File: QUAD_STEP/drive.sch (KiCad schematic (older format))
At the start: 17 parts, among them U3 TMC5160-TA

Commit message: beginning layout
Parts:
- C17: footprint (none) -> Capacitor_SMD:C_0603_1608Metric_Pad1.05x0.95mm_HandSolder
- C18: footprint (none) -> Capacitor_SMD:C_0603_1608Metric_Pad1.05x0.95mm_HandSolder; ALTERNATE (none) -> EMK107BJ225KA-T,587-1430-1-ND; DPN (none) -> 1276-1040-1-ND
- C20: footprint (none) -> CUSTOM:CAPAE1350X1400N_EEVFK1J151Q
- R86, R87, R88, R89, R90: footprint (none) -> Resistor_SMD:R_0603_1608Metric_Pad1.05x0.95mm_HandSolder
- U3: footprint eTQFP48_9x9 -> CUSTOM:TMC5160-TA; DPN (none) -> 1460-1249-ND; MPN (none) -> TMC5160-TA
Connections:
- net GND: now also C18.1; no longer C18.2
- net at U3.3 (12VOUT): now also C18.2; no longer C18.1

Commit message: complebegan adding 3D files
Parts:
- C16, C19: footprint Capacitor_SMD:C_0603_1608Metric -> Capacitor_SMD:C_0603_1608Metric_Pad1.05x0.95mm_HandSolder
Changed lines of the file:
@@
 AR Path="/5E50B0AB/5E4B8E3D" Ref="U5"  Part="1"
 AR Path="/5E50B60F/5E4B8E3D" Ref="U6"  Part="1"
-F 0 "U6" H 5400 1737 60  0000 C CNN
+F 0 "U3" H 5400 1737 60  0000 C CNN
 F 1 "TMC5160-TA" H 5400 1631 60  0000 C CNN
 F 2 "CUSTOM:TMC5160-TA" H 5400 1590 60  0001 C CNN
@@
 AR Path="/5E50B0AB/5E4B8E77" Ref="C60"  Part="1"
 AR Path="/5E50B60F/5E4B8E77" Ref="C77"  Part="1"
-F 0 "C77" H 7015 2296 50  0000 L CNN
+F 0 "C26" H 7015 2296 50  0000 L CNN
 F 1 "22n" H 7015 2205 50  0000 L CNN
 F 2 "Capacitor_SMD:C_0603_1608Metric" H 6938 2100 50  0001 C CNN
@@
 AR Path="/5E50B0AB/5E4B8EAA" Ref="#PWR067"  Part="1"
 AR Path="/5E50B60F/5E4B8EAA" Ref="#PWR083"  Part="1"
-F 0 "#PWR083" H 3500 3250 50  0001 C CNN
+F 0 "#PWR035" H 3500 3250 50  0001 C CNN
 F 1 "GND" V 3505 3372 50  0000 R CNN
 F 2 "" H 3500 3500 50  0001 C CNN
@@
 AR Path="/5E50B0AB/5E4B8EBB" Ref="C51"  Part="1"
 AR Path="/5E50B60F/5E4B8EBB" Ref="C68"  Part="1"
-F 0 "C68" H 3300 4150 50  0000 R BNN
+F 0 "C17" H 3300 4150 50  0000 R BNN
 F 1 "2u2" H 3300 4300 50  0000 R BNN
 F 2 "Capacitor_SMD:C_0603_1608Metric_Pad1.05x0.95mm_HandSolder" H 3338 4100 50  0001 C CNN
@@
 AR Path="/5E50B0AB/5E4B8EC5" Ref="C50"  Part="1"
 AR Path="/5E50B60F/5E4B8EC5" Ref="C67"  Part="1"
-F 0 "C67" H 2965 3996 50  0000 L CNN
+F 0 "C16" H 2965 3996 50  0000 L CNN
 F 1 "100n" H 2965 3905 50  0000 L CNN
-F 2 "Capacitor_SMD:C_0603_1608Metric" H 2888 3800 50  0001 C CNN
+F 2 "Capacitor_SMD:C_0603_1608Metric_Pad1.05x0.95mm_HandSolder" H 2888 3800 50  0001 C CNN
 F 3 "" H 2850 3950 50  0001 C CNN
 F 4 "06031C104KAT2A" H 2850 3950 50  0001 C CNN "MPN"
@@
 AR Path="/5E50B0AB/5E4B8ECF" Ref="C53"  Part="1"
 AR Path="/5E50B60F/5E4B8ECF" Ref="C70"  Part="1"
-F 0 "C70" H 4065 4296 50  0000 L CNN
+F 0 "C19" H 4065 4296 50  0000 L CNN
 F 1 "470n" H 4065 4205 50  0000 L CNN
-F 2 "Capacitor_SMD:C_0603_1608Metric" H 3988 4100 50  0001 C CNN
+F 2 "Capacitor_SMD:C_0603_1608Metric_Pad1.05x0.95mm_HandSolder" H 3988 4100 50  0001 C CNN
 F 3 "~" H 3950 4250 50  0001 C CNN
 F 4 "885012106008" H 3950 4250 50  0001 C CNN "MPN"
@@
 AR Path="/5E50B0AB/5E4B8ED9" Ref="C59"  Part="1"
 AR Path="/5E50B60F/5E4B8ED9" Ref="C76"  Part="1"
-F 0 "C76" H 7015 1646 50  0000 L CNN
+F 0 "C25" H 7015 1646 50  0000 L CNN
 F 1 "100n" H 7015 1555 50  0000 L CNN
 F 2 "Capacitor_SMD:C_0603_1608Metric" H 6938 1450 50  0001 C CNN
@@
 AR Path="/5E50B0AB/5E4B8EEC" Ref="#PWR065"  Part="1"
 AR Path="/5E50B60F/5E4B8EEC" Ref="#PWR081"  Part="1"
-F 0 "#PWR081" H 2850 3950 50  0001 C CNN
+F 0 "#PWR033" H 2850 3950 50  0001 C CNN
 F 1 "GND" H 2850 4100 50  0000 C TNN
 F 2 "" H 2850 4200 50  0001 C CNN
@@
 AR Path="/5E50B0AB/5E4B8EF7" Ref="R128"  Part="1"
 AR Path="/5E50B60F/5E4B8EF7" Ref="R147"  Part="1"
-F 0 "R147" V 3450 4050 50  0000 C CNN
+F 0 "R90" V 3450 4050 50  0000 C CNN
 F 1 "2R2" V 3650 4050 50  0000 C CNN
 F 2 "Resistor_SMD:R_0603_1608Metric_Pad1.05x0.95mm_HandSolder" V 3480 4050 50  0001 C CNN
@@
 AR Path="/5E50B0AB/5E4B8F02" Ref="#PWR068"  Part="1"
 AR Path="/5E50B60F/5E4B8F02" Ref="#PWR084"  Part="1"
-F 0 "#PWR084" H 3950 4250 50  0001 C CNN
+F 0 "#PWR036" H 3950 4250 50  0001 C CNN
 F 1 "GND" H 3950 4400 50  0000 C TNN
 F 2 "" H 3950 4500 50  0001 C CNN
@@
 AR Path="/5E50B0AB/5E4B8F08" Ref="#PWR066"  Part="1"
 AR Path="/5E50B60F/5E4B8F08" Ref="#PWR082"  Part="1"
-F 0 "#PWR082" H 3300 4250 50  0001 C CNN
+F 0 "#PWR034" H 3300 4250 50  0001 C CNN
 F 1 "GND" H 3300 4400 50  0000 C TNN
 F 2 "" H 3300 4500 50  0001 C CNN
@@
 AR Path="/5E50B0AB/5E4B8F16" Ref="#PWR069"  Part="1"
 AR Path="/5E50B60F/5E4B8F16" Ref="#PWR085"  Part="1"
-F 0 "#PWR085" H 4000 5250 50  0001 C CNN
+F 0 "#PWR037" H 4000 5250 50  0001 C CNN
 F 1 "GND" H 4000 5400 50  0000 C TNN
 F 2 "" H 4000 5500 50  0001 C CNN
@@
 AR Path="/5E50B0AB/5E4B8F3C" Ref="C54"  Part="1"
 AR Path="/5E50B60F/5E4B8F3C" Ref="C71"  Part="1"
-F 0 "C71" H 4518 6446 50  0000 L CNN
+F 0 "C20" H 4518 6446 50  0000 L CNN
 F 1 "150u 80V" H 4518 6355 50  0000 L CNN
 F 2 "CUSTOM:CAPAE1350X1400N_EEVFK1J151Q" H 4438 6250 50  0001 C CNN
@@
 AR Path="/5E50B0AB/5E4B8F46" Ref="C58"  Part="1"
 AR Path="/5E50B60F/5E4B8F46" Ref="C75"  Part="1"
-F 0 "C75" H 6465 6446 50  0000 L CNN
+F 0 "C24" H 6465 6446 50  0000 L CNN
 F 1 "100n" H 6465 6355 50  0000 L CNN
 F 2 "Capacitor_SMD:C_0603_1608Metric" H 6388 6250 50  0001 C CNN
@@
 AR Path="/5E50B0AB/5E4B8F50" Ref="C57"  Part="1"
 AR Path="/5E50B60F/5E4B8F50" Ref="C74"  Part="1"
-F 0 "C74" H 6015 6446 50  0000 L CNN
+F 0 "C23" H 6015 6446 50  0000 L CNN
 F 1 "100n" H 6015 6355 50  0000 L CNN
 F 2 "Capacitor_SMD:C_0603_1608Metric" H 5938 6250 50  0001 C CNN
@@
 AR Path="/5E50B0AB/5E4B8F5A" Ref="C55"  Part="1"
 AR Path="/5E50B60F/5E4B8F5A" Ref="C72"  Part="1"
-F 0 "C72" H 5165 6446 50  0000 L CNN
+F 0 "C21" H 5165 6446 50  0000 L CNN
 F 1 "10u" H 5165 6355 50  0000 L CNN
 F 2 "Capacitor_SMD:C_1210_3225Metric_Pad1.42x2.65mm_HandSolder" H 5088 6250 50  0001 C CNN
@@
 AR Path="/5E50B0AB/5E4B8F64" Ref="C56"  Part="1"
 AR Path="/5E50B60F/5E4B8F64" Ref="C73"  Part="1"
-F 0 "C73" H 5615 6446 50  0000 L CNN
+F 0 "C22" H 5615 6446 50  0000 L CNN
 F 1 "10u" H 5615 6355 50  0000 L CNN
 F 2 "Capacitor_SMD:C_1210_3225Metric_Pad1.42x2.65mm_HandSolder" H 5538 6250 50  0001 C CNN
@@
 AR Path="/5E50B0AB/5E4B8F88" Ref="#PWR070"  Part="1"
 AR Path="/5E50B60F/5E4B8F88" Ref="#PWR086"  Part="1"
-F 0 "#PWR086" H 4400 6350 50  0001 C CNN
+F 0 "#PWR038" H 4400 6350 50  0001 C CNN
 F 1 "GND" H 4400 6500 50  0000 C TNN
 F 2 "" H 4400 6600 50  0001 C CNN
@@
 AR Path="/5E50B0AB/5E4B8F8E" Ref="#PWR071"  Part="1"
 AR Path="/5E50B60F/5E4B8F8E" Ref="#PWR087"  Part="1"
-F 0 "#PWR087" H 5050 6350 50  0001 C CNN
+F 0 "#PWR039" H 5050 6350 50  0001 C CNN
 F 1 "GND" H 5050 6500 50  0000 C TNN
 F 2 "" H 5050 6600 50  0001 C CNN
@@
 AR Path="/5E50B0AB/5E4B8F94" Ref="#PWR072"  Part="1"
 AR Path="/5E50B60F/5E4B8F94" Ref="#PWR088"  Part="1"
-F 0 "#PWR088" H 5500 6350 50  0001 C CNN
+F 0 "#PWR040" H 5500 6350 50  0001 C CNN
 F 1 "GND" H 5500 6500 50  0000 C TNN
 F 2 "" H 5500 6600 50  0001 C CNN
@@
 AR Path="/5E50B0AB/5E4B8F9A" Ref="#PWR073"  Part="1"
 AR Path="/5E50B60F/5E4B8F9A" Ref="#PWR089"  Part="1"
-F 0 "#PWR089" H 5900 6350 50  0001 C CNN
+F 0 "#PWR041" H 5900 6350 50  0001 C CNN
 F 1 "GND" H 5900 6500 50  0000 C TNN
 F 2 "" H 5900 6600 50  0001 C CNN
@@
 AR Path="/5E50B0AB/5E4B8FA0" Ref="#PWR074"  Part="1"
 AR Path="/5E50B60F/5E4B8FA0" Ref="#PWR090"  Part="1"
-F 0 "#PWR090" H 6350 6350 50  0001 C CNN
+F 0 "#PWR042" H 6350 6350 50  0001 C CNN
 F 1 "GND" H 6350 6500 50  0000 C TNN
 F 2 "" H 6350 6600 50  0001 C CNN
@@
 AR Path="/5E50B0AB/5E4B8FAE" Ref="R126"  Part="1"
 AR Path="/5E50B60F/5E4B8FAE" Ref="R145"  Part="1"
-F 0 "R145" V 1650 2400 50  0000 C CNN
+F 0 "R88" V 1650 2400 50  0000 C CNN
 F 1 "DNP" V 1850 2400 50  0000 C CNN
 F 2 "Resistor_SMD:R_0603_1608Metric_Pad1.05x0.95mm_HandSolder" V 1680 2400 50  0001 C CNN
@@
 AR Path="/5E50B0AB/5E4B8FC3" Ref="R127"  Part="1"
 AR Path="/5E50B60F/5E4B8FC3" Ref="R146"  Part="1"
-F 0 "R146" V 1650 2800 50  0000 C CNN
+F 0 "R89" V 1650 2800 50  0000 C CNN
 F 1 "0R" V 1850 2800 50  0000 C CNN
 F 2 "Resistor_SMD:R_0603_1608Metric_Pad1.05x0.95mm_HandSolder" V 1680 2800 50  0001 C CNN
@@
 AR Path="/5E50B0AB/5E4B8FD0" Ref="R124"  Part="1"
 AR Path="/5E50B60F/5E4B8FD0" Ref="R143"  Part="1"
-F 0 "R143" V 1200 1700 50  0000 C CNN
+F 0 "R86" V 1200 1700 50  0000 C CNN
 F 1 "0R" V 1400 1700 50  0000 C CNN
 F 2 "Resistor_SMD:R_0603_1608Metric_Pad1.05x0.95mm_HandSolder" V 1230 1700 50  0001 C CNN
@@
 AR Path="/5E50B0AB/5E4B8FDA" Ref="R125"  Part="1"
 AR Path="/5E50B60F/5E4B8FDA" Ref="R144"  Part="1"
-F 0 "R144" V 1200 2100 50  0000 C CNN
+F 0 "R87" V 1200 2100 50  0000 C CNN
 F 1 "DNP" V 1400 2100 50  0000 C CNN
 F 2 "Resistor_SMD:R_0603_1608Metric_Pad1.05x0.95mm_HandSolder" V 1230 2100 50  0001 C CNN
@@
 AR Path="/5E50B0AB/5E4B8FE1" Ref="#PWR064"  Part="1"
 AR Path="/5E50B60F/5E4B8FE1" Ref="#PWR080"  Part="1"
-F 0 "#PWR080" H 1750 2750 50  0001 C CNN
+F 0 "#PWR032" H 1750 2750 50  0001 C CNN
 F 1 "GND" H 1750 2900 50  0000 C TNN
 F 2 "" H 1750 3000 50  0001 C CNN
@@
 AR Path="/5E50B0AB/5E4B8FE7" Ref="#PWR063"  Part="1"
 AR Path="/5E50B60F/5E4B8FE7" Ref="#PWR079"  Part="1"
-F 0 "#PWR079" H 1300 2050 50  0001 C CNN
+F 0 "#PWR031" H 1300 2050 50  0001 C CNN
 F 1 "GND" H 1300 2200 50  0000 C TNN
 F 2 "" H 1300 2300 50  0001 C CNN
@@
 AR Path="/5E50B0AB/5E8C27DD" Ref="C52"  Part="1"
 AR Path="/5E50B60F/5E8C27DD" Ref="C69"  Part="1"
-F 0 "C69" V 3850 3450 50  0000 R BNN
+F 0 "C18" V 3850 3450 50  0000 R BNN
 F 1 "2u2" V 3850 3700 50  0000 R BNN
 F 2 "Capacitor_SMD:C_0603_1608Metric_Pad1.05x0.95mm_HandSolder" H 3838 3350 50  0001 C CNN

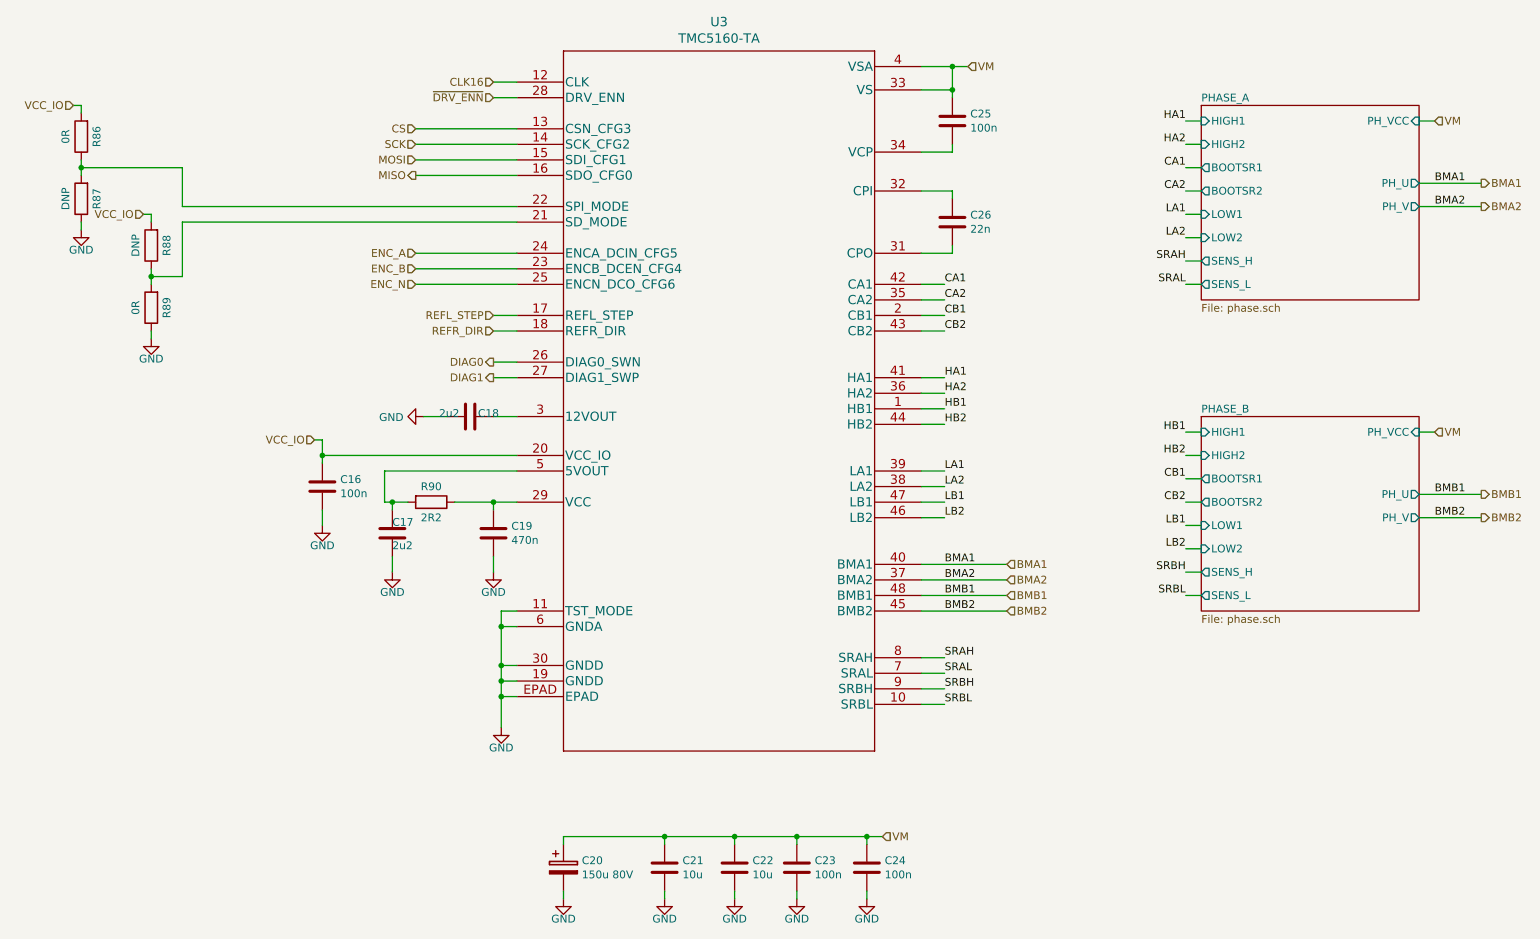
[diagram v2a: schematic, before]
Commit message: changed scope to 5 axis, preliminary completion of component positioning
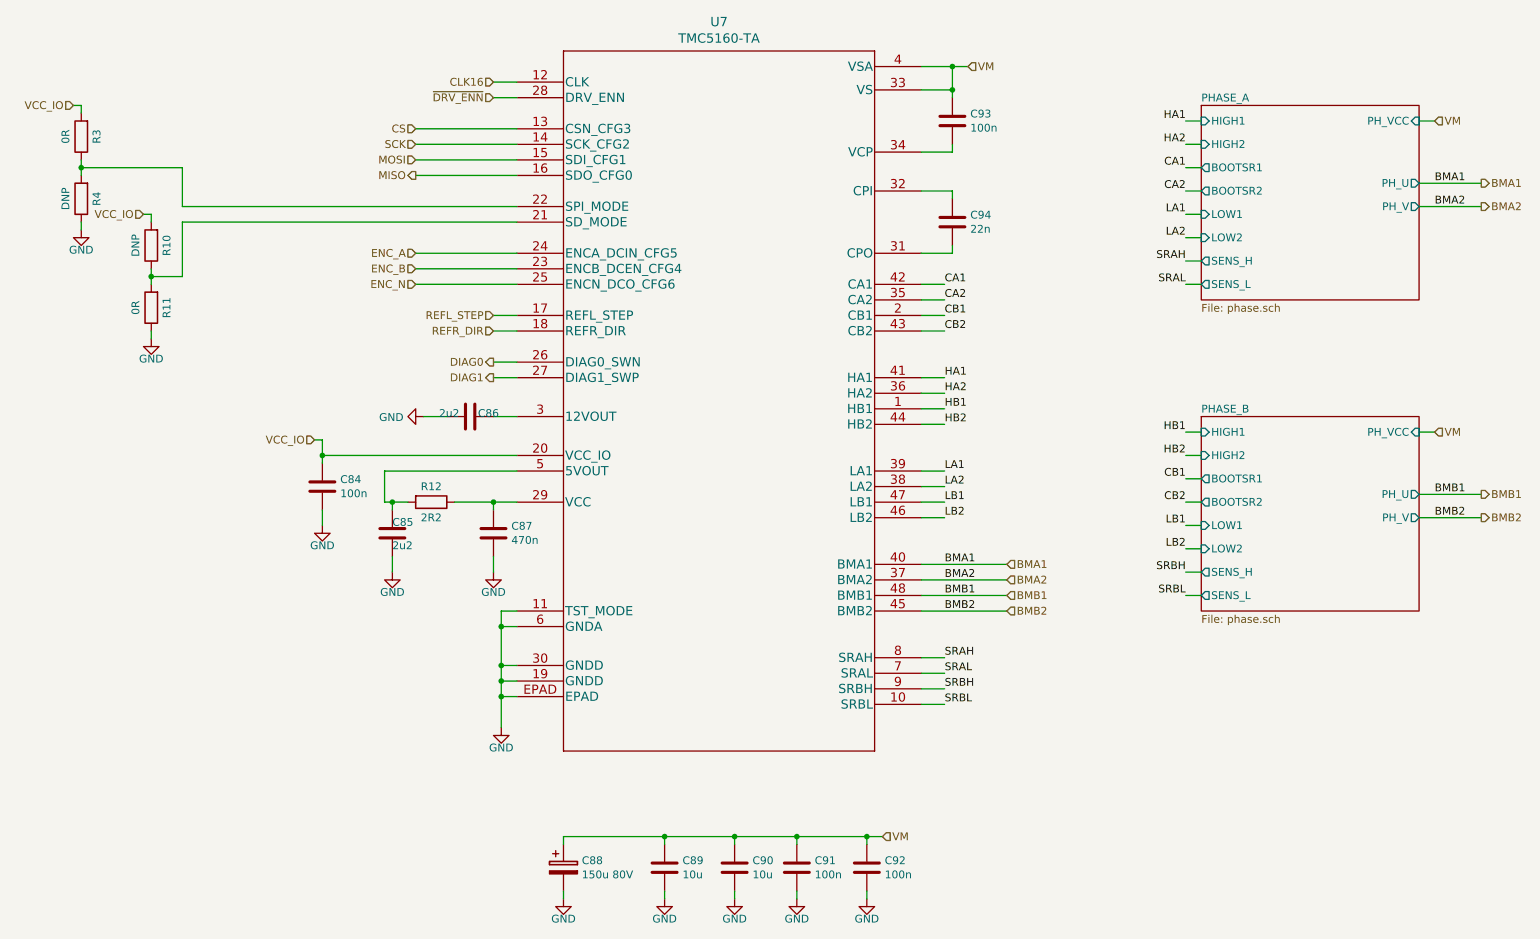
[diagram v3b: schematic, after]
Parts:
- C20: footprint CUSTOM:CAPAE1350X1400N_EEVFK1J151Q -> CUSTOM_FP:CAPAE1350X1400N_EEVFK1J151Q
- U3: footprint CUSTOM:TMC5160-TA -> CUSTOM_FP:TMC5160-TA
